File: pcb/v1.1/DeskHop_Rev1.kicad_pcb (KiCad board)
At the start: 2 copper layers, 66.9 x 74.5 mm, 20 parts, among them J1 Keyboard In, J2 Debug2, J3 Debug1, J4 Mouse In, U2 Pico Primary Custom, U3 TPD4E1U06DBVR, U4 ADuM1201BR, U5 TPD4E1U06DBVR, U6 Pico Primary Custom

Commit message: somewhat verOneZeroOne
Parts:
- moved C2 15.4 mm to (70.6, 84.0), turned to 90 degrees
- moved C1 9.27 mm to (64.7, 84.1), turned to 90 degrees
- moved U4 5.06 mm to (67.9, 89.5)
- moved R1 3.00 mm to (75.4, 97.6)
- moved R2 2.98 mm to (72.4, 97.6)
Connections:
- C1 pad 1: 3V3_BUS2 -> 3V3
- C1 pad 2: GND -> GND1
- C3 pad 2: GND -> GND1
- J2 pad 1: unconnected-(J2-Pin_1-Pad1) -> Net-(J2-Pin_1)
- J2 pad 2: GND -> Net-(J2-Pin_2)
- J2 pad 3: unconnected-(J2-Pin_3-Pad3) -> Net-(J2-Pin_3)
- J3 pad 1: unconnected-(J3-Pin_1-Pad1) -> Net-(J3-Pin_1)
- J3 pad 2: GND2 -> Net-(J3-Pin_2)
- J3 pad 3: unconnected-(J3-Pin_3-Pad3) -> Net-(J3-Pin_3)
- J4 pad 4: GND -> GND1
- J4 pad 5: GND -> GND1
- R3 pad 1: Net-(U2-GPIO15) -> Net-(U2-GPIO17)
- R4 pad 1: Net-(U2-GPIO14) -> Net-(U2-GPIO16)
- U2 pad 1: GND -> unconnected-(U2-GPIO0-Pad1)
- U2 pad 11: GND -> unconnected-(U2-GPIO9-Pad11)
- U2 pad 15: unconnected-(U2-GND-Pad15) -> GND1
- U2 pad 16: GND -> unconnected-(U2-GPIO13-Pad16)
- U2 pad 17: Net-(U2-GPIO14) -> unconnected-(U2-GPIO14-Pad17)
- U2 pad 18: Net-(U2-GPIO15) -> unconnected-(U2-GPIO15-Pad18)
- U2 pad 19: unconnected-(U2-GPIO16-Pad19) -> Net-(U2-GPIO16)
- U2 pad 20: unconnected-(U2-GPIO17-Pad20) -> Net-(U2-GPIO17)
- U2 pad 21: unconnected-(U2-GPIO18-Pad21) -> UART B TX
- U2 pad 22: unconnected-(U2-GPIO19-Pad22) -> UART B RX
- U2 pad 23: UART B TX -> unconnected-(U2-GPIO20-Pad23)
- U2 pad 24: UART B RX -> unconnected-(U2-GPIO21-Pad24)
- U2 pad 25: GND -> unconnected-(U2-GPIO22-Pad25)
- U2 pad 30: GND -> unconnected-(U2-GPIO26-Pad30)
- U2 pad 36: unconnected-(U2-3V3-Pad36) -> 3V3
- U2 pad 38: 3V3_BUS2 -> unconnected-(U2-GND-Pad38)
- U2 pad 40: GND -> VBUS2
- U2 pad 41: unconnected-(U2-SWCLK-Pad41) -> Net-(J2-Pin_3)
- U2 pad 42: unconnected-(U2-GND-Pad42) -> Net-(J2-Pin_2)
- U2 pad 43: unconnected-(U2-SWDIO-Pad43) -> Net-(J2-Pin_1)
- U2 pad 6: GND -> GND1
- U4 pad 1: 3V3_BUS2 -> 3V3
- U4 pad 4: GND -> GND1
- U5 pad 2: GND -> GND1
- U6 pad 1: GND2 -> unconnected-(U6-GPIO0-Pad1)
- U6 pad 11: GND2 -> unconnected-(U6-GPIO9-Pad11)
- U6 pad 14: UART A TX -> unconnected-(U6-GPIO12-Pad14)
- U6 pad 15: UART A RX -> GND2
- U6 pad 16: GND2 -> unconnected-(U6-GPIO13-Pad16)
- U6 pad 17: /AD+ -> UART A TX
- U6 pad 18: /AD- -> UART A RX
- U6 pad 19: unconnected-(U6-GPIO16-Pad19) -> /AD+
- U6 pad 2: GND2 -> unconnected-(U6-GPIO1-Pad2)
- U6 pad 20: unconnected-(U6-GPIO17-Pad20) -> /AD-
- U6 pad 21: GND2 -> unconnected-(U6-GPIO18-Pad21)
- U6 pad 25: GND2 -> unconnected-(U6-GPIO22-Pad25)
- U6 pad 30: GND2 -> unconnected-(U6-GPIO26-Pad30)
- U6 pad 35: unconnected-(U6-GND-Pad35) -> GND2
- U6 pad 36: unconnected-(U6-3V3-Pad36) -> Net-(U4-VDD2)
- U6 pad 38: Net-(U4-VDD2) -> GND2
- U6 pad 40: GND2 -> VBUS1
- U6 pad 41: unconnected-(U6-SWCLK-Pad41) -> Net-(J3-Pin_3)
- U6 pad 42: unconnected-(U6-GND-Pad42) -> Net-(J3-Pin_2)
- U6 pad 43: unconnected-(U6-SWDIO-Pad43) -> Net-(J3-Pin_1)
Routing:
- net 3V3: track 0.00 -> 70.6 mm, vias 0 -> 1
- net VBUS2: track 101.4 -> 71.2 mm
- net unconnected-(U2-3V3-Pad36): track 24.8 -> 0.00 mm
- net Net-(J3-Pin_3): track 0.00 -> 19.5 mm
- net Net-(J2-Pin_3): track 0.00 -> 19.3 mm
- net Net-(J3-Pin_2): track 0.00 -> 18.4 mm
- net Net-(J2-Pin_2): track 0.00 -> 16.4 mm
- net VBUS1: track 93.5 -> 77.8 mm
- net Net-(U2-GPIO14): track 13.8 -> 0.00 mm
- net Net-(U4-VDD2): track 85.2 -> 71.9 mm, vias 0 -> 2
- net Net-(U2-GPIO15): track 12.5 -> 0.00 mm
- net Net-(J2-Pin_1): track 0.00 -> 12.3 mm
- net Net-(J3-Pin_1): track 0.00 -> 12.2 mm
- net OA-: track 22.0 -> 11.7 mm
- net 3V3_BUS2: track 8.82 -> 0.00 mm
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- added copper zone on F.Cu, net GND1
- added copper zone on F.Cu, net unconnected-(U2-GPIO22-Pad25)
- removed copper zone on F.Cu, net GND
- removed copper zone on B.Cu, net GND2
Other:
- board text added: "GND*"
- board text removed: "${REFERENCE}"

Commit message: ver OneXeroOne
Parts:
- removed J2: Debug2, Connector_PinHeader_2.54mm:PinHeader_1x03_P2.54mm_Vertical
- removed J3: Debug1, Connector_PinHeader_2.54mm:PinHeader_1x03_P2.54mm_Vertical
- removed U3: TPD4E1U06DBVR, Library:TPD4E1U06DBVR
- added U1: TPD4E1U06DBVR, Customs:DBV6_TEX, F.Cu at (173.4, 100.7)
- U5: footprint Library:TPD4E1U06DBVR -> Customs:DBV6_TEX
- moved H3 134.5 mm to (178.0, 121.6)
- moved H1 121.6 mm to (140.9, 47.0)
- moved R2 95.5 mm to (167.9, 100.7)
- moved R1 87.7 mm to (163.1, 100.7)
- moved C4 85.3 mm to (158.3, 100.7)
- moved J1 81.1 mm to (161.9, 108.5)
- moved U5 80.9 mm to (124.3, 100.7)
- moved U6 79.9 mm to (165.2, 70.6)
- moved R4 78.8 mm to (118.7, 100.7)
- moved R3 77.3 mm to (113.9, 100.7)
- moved C2 74.2 mm to (144.0, 73.3), turned to 0 degrees
- moved C1 73.8 mm to (137.7, 73.3), turned to 180 degrees
- moved U4 73.6 mm to (140.8, 79.6)
- moved C3 70.5 mm to (109.1, 100.7)
- moved J4 67.3 mm to (112.8, 108.5)
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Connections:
- H1 pad 1: GND -> GND2
- H2 pad 1: GND2 -> GND1
- U2 pad 21: UART B TX -> unconnected-(U2-GPIO18-Pad21)
- U2 pad 22: UART B RX -> unconnected-(U2-GPIO19-Pad22)
- U2 pad 26: unconnected-(U2-GPIO23-Pad26) -> UART B TX
- U2 pad 27: unconnected-(U2-GPIO24-Pad27) -> UART B RX
- U2 pad 41: Net-(J2-Pin_3) -> unconnected-(U2-SWCLK-Pad41)
- U2 pad 42: Net-(J2-Pin_2) -> unconnected-(U2-GND-Pad42)
- U2 pad 43: Net-(J2-Pin_1) -> unconnected-(U2-SWDIO-Pad43)
- U6 pad 13: unconnected-(U6-GPIO11-Pad13) -> UART A TX
- U6 pad 14: unconnected-(U6-GPIO12-Pad14) -> UART A RX
- U6 pad 17: UART A TX -> unconnected-(U6-GPIO14-Pad17)
- U6 pad 18: UART A RX -> unconnected-(U6-GPIO15-Pad18)
- U6 pad 41: Net-(J3-Pin_3) -> unconnected-(U6-SWCLK-Pad41)
- U6 pad 42: Net-(J3-Pin_2) -> unconnected-(U6-GND-Pad42)
- U6 pad 43: Net-(J3-Pin_1) -> unconnected-(U6-SWDIO-Pad43)
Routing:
- net 3V3: track 70.6 -> 27.8 mm, vias 1 -> 0
- net Net-(J3-Pin_3): track 19.5 -> 0.00 mm
- net Net-(J2-Pin_3): track 19.3 -> 0.00 mm
- net Net-(J3-Pin_2): track 18.4 -> 0.00 mm
- net Net-(J2-Pin_2): track 16.4 -> 0.00 mm
- net Net-(U2-GPIO16): track 7.35 -> 21.8 mm
- net /AD+: track 8.26 -> 21.7 mm
- net Net-(J2-Pin_1): track 12.3 -> 0.00 mm
- net Net-(J3-Pin_1): track 12.2 -> 0.00 mm
- net OA-: track 11.7 -> 20.8 mm
- net GND2: track 0.00 -> 8.26 mm
- net UART A RX: track 7.66 -> 14.5 mm
- net OA+: track 20.3 -> 13.8 mm
- net VBUS2: track 71.2 -> 77.2 mm, vias 0 -> 1
- net UART B RX: track 7.64 -> 13.6 mm
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- removed copper zone on F.Cu, net unconnected-(U2-GPIO22-Pad25)
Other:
- board size 66.9 x 74.5 mm -> 81.7 x 81.6 mm
- board text removed: "*"
- board text removed: "A"
- board text removed: "B"
- board text removed: "CLK"
- board text removed: "DATA"
- board text removed: "DeskHop"
- board text removed: "GND"
- board text removed: "GND*"
- board text removed: "Keyboard/Mouse Switch"
- board text removed: "OUT A"
- board text removed: "OUT B"
- board text removed: "by Hrvoje Cavrak, 01/24"
- board text removed: "https://github.com/hrvach"
- board text removed: "rev 1.1"

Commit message: updates
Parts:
- moved H2 8.71 mm to (103.6, 112.9)
- moved H3 8.24 mm to (177.8, 113.3)
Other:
- board size 81.7 x 81.6 mm -> 81.7 x 74 mm
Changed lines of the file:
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@@
 	(footprint "MountingHole:MountingHole_2.7mm_M2.5_Pad_TopBottom"
 		(layer "F.Cu")
-		(at 177.997 121.565033)
+		(at 177.759 113.331033)
 		(descr "Mounting Hole 2.7mm, M2.5")
 		(tags "mounting hole 2.7mm m2.5")
@@
 	(footprint "MountingHole:MountingHole_2.7mm_M2.5_Pad_TopBottom"
 		(layer "F.Cu")
-		(at 103.575 121.565033)
+		(at 103.619 112.851033)
 		(descr "Mounting Hole 2.7mm, M2.5")
 		(tags "mounting hole 2.7mm m2.5")
@@
 	(gr_rect
 		(start 99.999 43.161033)
-		(end 181.649 124.781033)
+		(end 181.649 117.161033)
 		(stroke
 			(width 0.05)
@@
 		(polygon
 			(pts
-				(xy 100.527 43.841033) (xy 139.897 43.841033) (xy 139.897 124.613033) (xy 100.527 124.613033)
+				(xy 100.527 43.841033) (xy 139.897 43.841033) (xy 139.527 116.743033) (xy 100.157 116.743033)
 			)
 		)
@@
 		(polygon
 			(pts
-				(xy 141.929 43.841033) (xy 181.045 43.841033) (xy 181.045 124.359033) (xy 141.929 124.359033)
+				(xy 141.929 43.841033) (xy 181.045 43.841033) (xy 181.175 116.979033) (xy 142.059 116.979033)
 			)
 		)

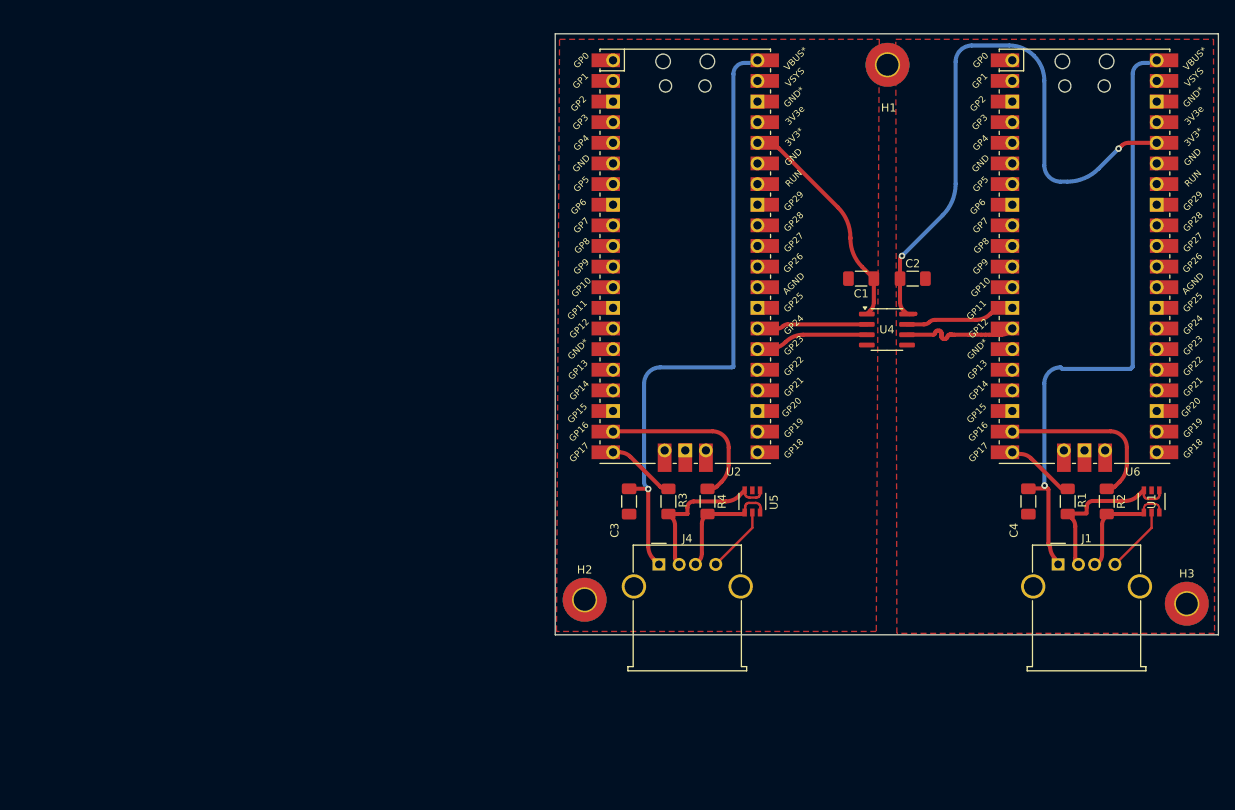
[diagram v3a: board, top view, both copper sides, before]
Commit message: match pins to original board
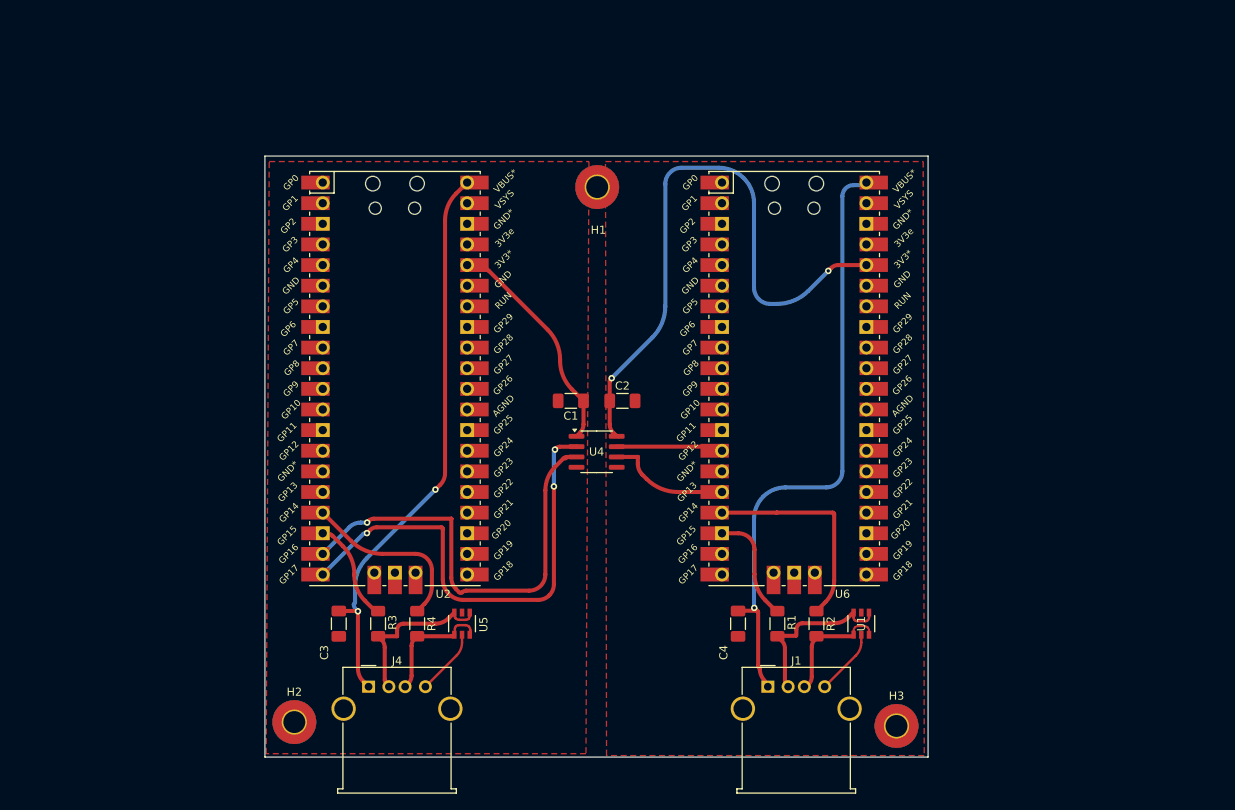
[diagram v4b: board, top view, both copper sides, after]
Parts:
- moved R2 38.8 mm to (132.2, 115.8)
- moved U1 38.8 mm to (137.7, 115.8)
- moved U4 38.8 mm to (105.1, 94.6)
- moved C1 38.8 mm to (101.9, 88.4)
- moved C3 38.8 mm to (73.4, 115.8)
- moved C4 38.8 mm to (122.5, 115.8)
- moved H2 38.8 mm to (67.9, 127.9)
- moved J1 38.8 mm to (126.2, 123.5)
- moved J4 38.8 mm to (77.0, 123.5)
- moved R1 38.8 mm to (127.3, 115.8)
- moved R3 38.8 mm to (78.2, 115.8)
- moved R4 38.8 mm to (83.0, 115.8)
- moved U2 38.8 mm to (80.3, 85.6)
- moved U5 38.8 mm to (88.5, 115.8)
- moved C2 38.8 mm to (108.3, 88.4)
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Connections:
- R1 pad 1: /AD- -> Net-(U6-GPIO15)
- R3 pad 1: Net-(U2-GPIO17) -> Net-(U2-GPIO15)
- R4 pad 1: Net-(U2-GPIO16) -> Net-(U2-GPIO14)
- U2 pad 17: unconnected-(U2-GPIO14-Pad17) -> Net-(U2-GPIO14)
- U2 pad 18: unconnected-(U2-GPIO15-Pad18) -> Net-(U2-GPIO15)
- U2 pad 19: Net-(U2-GPIO16) -> UART B TX
- U2 pad 20: Net-(U2-GPIO17) -> UART B RX
- U2 pad 26: UART B TX -> unconnected-(U2-GPIO23-Pad26)
- U2 pad 27: UART B RX -> unconnected-(U2-GPIO24-Pad27)
- U2 pad 35: unconnected-(U2-GND-Pad35) -> GND1
- U2 pad 38: unconnected-(U2-GND-Pad38) -> GND1
- U2 pad 42: unconnected-(U2-GND-Pad42) -> GND1
- U6 pad 13: UART A TX -> unconnected-(U6-GPIO11-Pad13)
- U6 pad 14: UART A RX -> UART A TX
- U6 pad 16: unconnected-(U6-GPIO13-Pad16) -> UART A RX
- U6 pad 17: unconnected-(U6-GPIO14-Pad17) -> /AD+
- U6 pad 18: unconnected-(U6-GPIO15-Pad18) -> Net-(U6-GPIO15)
- U6 pad 19: /AD+ -> unconnected-(U6-GPIO16-Pad19)
- U6 pad 20: /AD- -> unconnected-(U6-GPIO17-Pad20)
- U6 pad 42: unconnected-(U6-GND-Pad42) -> GND2
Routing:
- net UART B RX: track 13.6 -> 59.0 mm, vias 0 -> 3
- net UART B TX: track 13.9 -> 55.4 mm, vias 0 -> 1
- net Net-(U2-GPIO14): track 0.00 -> 22.2 mm
- net Net-(U2-GPIO16): track 21.8 -> 0.00 mm
- net Net-(U6-GPIO15): track 0.00 -> 13.7 mm
- net Net-(U2-GPIO15): track 0.00 -> 12.6 mm
- net Net-(U2-GPIO17): track 8.55 -> 0.00 mm
- net /AD-: track 7.49 -> 0.00 mm
- net VBUS2: track 77.2 -> 70.9 mm, vias 1 -> 2
- net /AD+: track 21.7 -> 27.0 mm
- net VBUS1: track 76.4 -> 74.4 mm
- net unconnected-(U2-GPIO23-Pad26): track 0.00 -> 1.34 mm
- net unconnected-(U6-GPIO11-Pad13): track 0.00 -> 0.98 mm
- net UART A RX: track 14.5 -> 15.4 mm
- net Net-(U4-VDD2): track 76.3 -> 75.6 mm
